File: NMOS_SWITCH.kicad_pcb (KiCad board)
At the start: 2 copper layers, 35 x 25 mm, 22 parts, among them J1 Conn_01x02, J2 Conn_01x02, J3 Conn_01x02, Q1 Q_NPN_BCE, Q2 CSD18540Q5B, U1 BTS443P, U2 LM5050-1

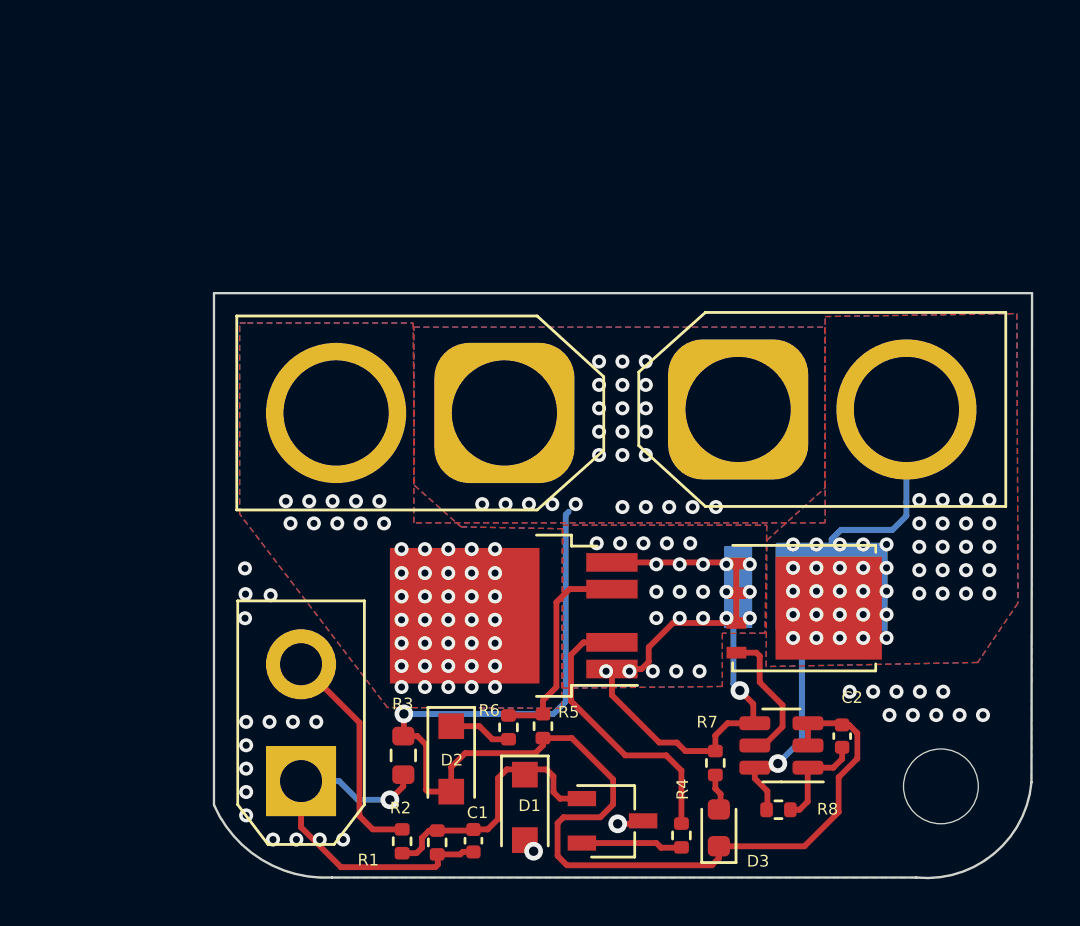
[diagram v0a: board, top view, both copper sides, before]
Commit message: Use LM5060, and update PCB
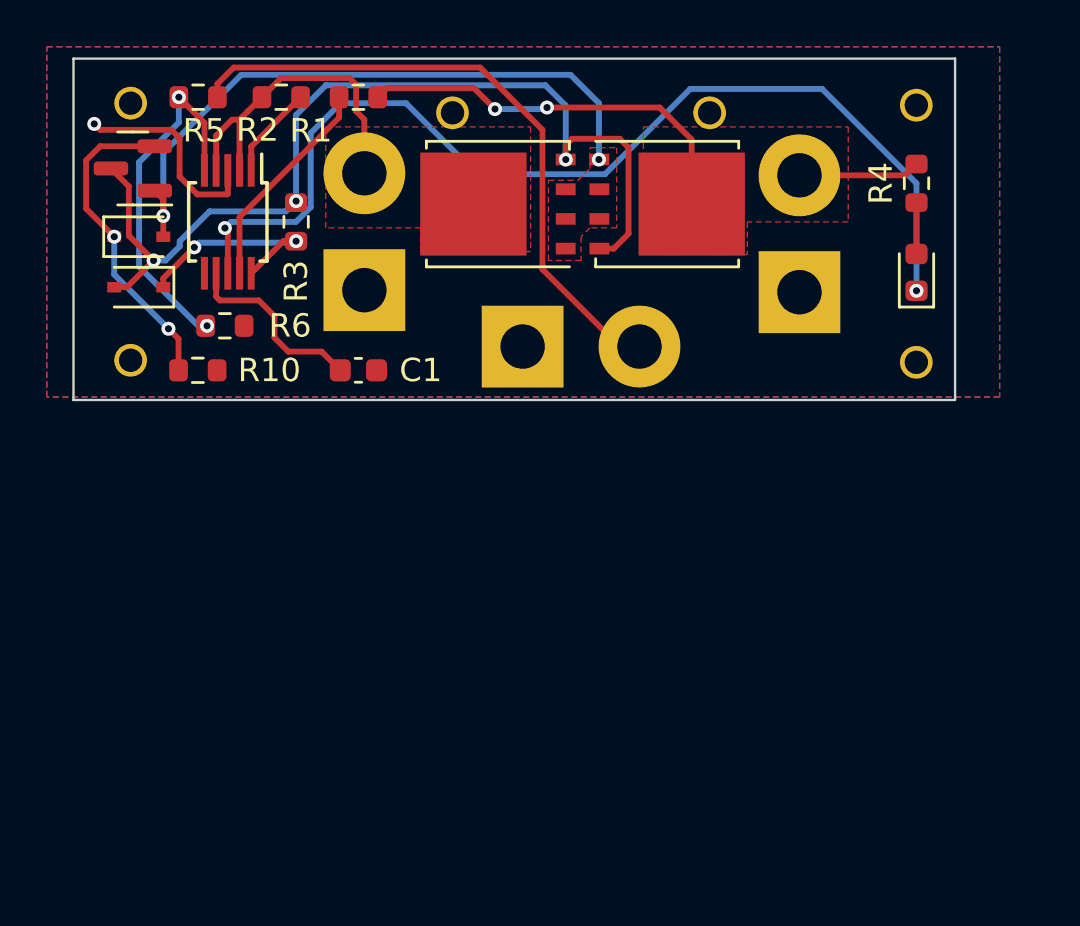
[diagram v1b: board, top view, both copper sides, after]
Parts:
- removed C2: 104, Capacitor_SMD:C_0402_1005Metric
- removed D4: SVM1550UB, POWER_DIODE_SMD:TO-277A
- removed H1: MountingHole, MountingHole:MountingHole_3.2mm_M3
- removed J1: Conn_01x02, Connector_AMASS:AMASS_XT30UPB-M_1x02_P5.0mm_Vertical
- removed R7: 10k, Resistor_SMD:R_0402_1005Metric
- removed R8: 100R, Resistor_SMD:R_0402_1005Metric
- removed U2: LM5050-1, Package_TO_SOT_SMD:TSOT-23-6
- added J4: Conn_01x02, Connector_AMASS:AMASS_XT30PW-M_1x02_P2.50mm_Horizontal, B.Cu at (151.8, 84.7)
- added Q3: S8050, Package_TO_SOT_SMD:SOT-23, F.Cu at (135.1, 77.1)
- added R10: 10k, Resistor_SMD:R_0603_1608Metric, F.Cu at (137.9, 85.7)
- C1: value 104 -> 68n; footprint Capacitor_SMD:C_0402_1005Metric -> Capacitor_SMD:C_0603_1608Metric
- D1: value BZT52Bxx -> 1N4001; footprint Diode_SMD:D_SOD-123F -> Diode_SMD:D_SOD-323
- D2: value BZT52Bxx -> LED; footprint Diode_SMD:D_SOD-123F -> LED_SMD:LED_0603_1608Metric
- D3: value LED -> 1N4001; footprint LED_SMD:LED_0603_1608Metric -> Diode_SMD:D_SOD-323
- J2: footprint Connector_AMASS:AMASS_XT60-M_1x02_P7.20mm_Vertical -> Connector_AMASS:AMASS_XT30PW-M_1x02_P2.50mm_Horizontal; moved to B.Cu
- J3: footprint Connector_AMASS:AMASS_XT60-F_1x02_P7.20mm_Vertical -> Connector_AMASS:AMASS_XT30PW-F_1x02_P2.50mm_Horizontal; moved to B.Cu
- Q1: value Q_NPN_BCE -> CSD18540Q5B; footprint Package_TO_SOT_SMD:TSOT-23 -> Package_TO_SOT_SMD:TDSON-8-1
- R1, R2, R5: footprint Resistor_SMD:R_0402_1005Metric -> Resistor_SMD:R_0603_1608Metric
- R3: value 0 -> 2k
- R4: value 10k -> 10K; footprint Resistor_SMD:R_0402_1005Metric -> Resistor_SMD:R_0603_1608Metric
- R6: value 2k -> 20k; footprint Resistor_SMD:R_0402_1005Metric -> Resistor_SMD:R_0603_1608Metric
- U1: value BTS443P -> LM5060; footprint Package_TO_SOT_SMD:TO-252-4 -> Package_SO:MSOP-10_3x3mm_P0.5mm
- moved D3 35.4 mm to (135.4, 80.0), turned to 0 degrees
- moved R2 32.6 mm to (141.5, 74.0), turned to 0 degrees
- moved R1 31.9 mm to (144.8, 74.0), turned to 180 degrees
- moved R5 30.7 mm to (137.9, 74.0), turned to 180 degrees
- moved R4 29.7 mm to (168.7, 77.7), turned to -90 degrees
- moved D2 28.8 mm to (168.7, 81.5), turned to 90 degrees
- moved D1 27.7 mm to (135.4, 82.2), turned to 180 degrees
- moved Q1 26.8 mm to (150.7, 78.6), turned to 180 degrees
- moved R3 23.3 mm to (142.1, 79.4)
- moved R6 21.0 mm to (139.1, 83.8), turned to 180 degrees
- moved U1 20.8 mm to (139.2, 79.4), turned to -90 degrees
- moved C1 20.7 mm to (144.8, 85.7), turned to 0 degrees
- moved Q2 18.3 mm to (158.0, 78.6)
- moved J2 7.97 mm to (145.0, 82.3), turned to -90 degrees
- moved J3 5.66 mm to (163.6, 82.4), turned to 90 degrees
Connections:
- D1 pad 1: Net-(C1-Pad1) -> Net-(D1-Pad1)
- D1 pad 2: GND -> Net-(D1-Pad2)
- D2 pad 1: Net-(R6-Pad2) -> /PGD
- D2 pad 2: GNDPWR -> Net-(D2-Pad2)
- D3 pad 1: GNDPWR -> Net-(D3-Pad1)
- J2 pad 1: GNDPWR -> GND
- J3 pad 1: GNDPWR -> GND
- Q1 pad 1: Net-(C1-Pad1) -> Net-(D3-Pad2)
- Q1 pad 2: Net-(Q1-Pad2) -> Net-(D3-Pad2)
- Q1 pad 3: GND -> Net-(D3-Pad2)
- Q2 pad 1: Net-(Q2-Pad1) -> Net-(D3-Pad2)
- Q2 pad 2: Net-(Q2-Pad1) -> Net-(D3-Pad2)
- Q2 pad 3: Net-(Q2-Pad1) -> Net-(D3-Pad2)
- Q2 pad 4: Net-(Q2-Pad4) -> Net-(D1-Pad2)
- R1 pad 1: /EN -> /NMOS_OUT
- R1 pad 2: Net-(C1-Pad1) -> Net-(R1-Pad2)
- R2 pad 1: Net-(C1-Pad1) -> /NMOS_IN
- R2 pad 2: GND -> Net-(R2-Pad2)
- R3 pad 1: GND -> Net-(D1-Pad1)
- R3 pad 2: GNDPWR -> Net-(D1-Pad2)
- R4 pad 1: Net-(Q1-Pad2) -> /NMOS_OUT
- R4 pad 2: Net-(R4-Pad2) -> Net-(D2-Pad2)
- R5 pad 1: GNDPWR -> Net-(J4-Pad2)
- R5 pad 2: Net-(R5-Pad2) -> /EN
- R6 pad 1: Net-(R5-Pad2) -> GND
- R6 pad 2: Net-(R6-Pad2) -> /EN
- U1 pad 1: Net-(Q2-Pad1) -> Net-(R2-Pad2)
- U1 pad 2: Net-(R4-Pad2) -> /NMOS_IN
- U1 pad 3: /NMOS_IN -> GND
- U1 pad 4: Net-(R5-Pad2) -> /NMOS_IN
- U1 pad 5: Net-(Q2-Pad1) -> /EN
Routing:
- net GNDPWR: track 55.5 -> 0.00 mm, vias 26 -> 0
- net /PGD: track 0.00 -> 44.7 mm, vias 0 -> 2
- net Net-(D1-Pad2): track 0.00 -> 41.3 mm, vias 0 -> 3
- net Net-(Q2-Pad1): track 28.0 -> 0.00 mm, vias 26 -> 0
- net Net-(J4-Pad2): track 0.00 -> 27.4 mm
- net Net-(D3-Pad2): track 1.60 -> 27.8 mm, vias 0 -> 2
- net /NMOS_IN: track 0.00 -> 14.7 mm, vias 45 -> 0
- net Net-(D3-Pad1): track 0.00 -> 13.8 mm, vias 0 -> 2
- net Net-(R4-Pad2): track 12.2 -> 0.00 mm
- net Net-(R1-Pad2): track 0.00 -> 9.30 mm
- net Net-(D1-Pad1): track 0.00 -> 9.21 mm, vias 0 -> 2
- net Net-(R5-Pad2): track 9.13 -> 0.00 mm
- net GND: track 17.2 -> 8.94 mm, vias 29 -> 1
- net Net-(Q2-Pad4): track 6.01 -> 0.00 mm
- net /EN: track 9.59 -> 15.5 mm, vias 0 -> 2
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- added copper zone on F.Cu, net Net-(D3-Pad2)
- removed copper zone on B.Cu, net /NMOS_IN
- removed copper zone on B.Cu, net /NMOS_OUT
- removed copper zone on B.Cu, net GNDPWR
- removed copper zone on F.Cu, net GNDPWR
- removed copper zone on B.Cu, net Net-(Q2-Pad1)
- removed copper zone on F.Cu, net Net-(Q2-Pad1)
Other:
- board size 35 x 25 mm -> 37.7 x 14.6 mm
